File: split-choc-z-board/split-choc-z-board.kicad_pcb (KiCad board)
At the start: 2 copper layers, 122.3 x 98.6 mm, 45 parts, among them J1 USB4105-GF-A, SW1 SW_SPST, SW10 SW_SPST, SW11 SW_SPST, SW12 SW_SPST, SW13 SW_SPST, SW14 SW_SPST, SW15 SW_SPST, SW16 SW_SPST, SW17 SW_SPST, SW18 SW_SPST, SW2 SW_SPST, SW3 SW_SPST, SW4 SW_SPST, SW5 SW_SPST, SW6 SW_SPST, SW7 SW_SPST, SW8 SW_SPST, SW9 SW_SPST, U1 USBLC6-2SC6

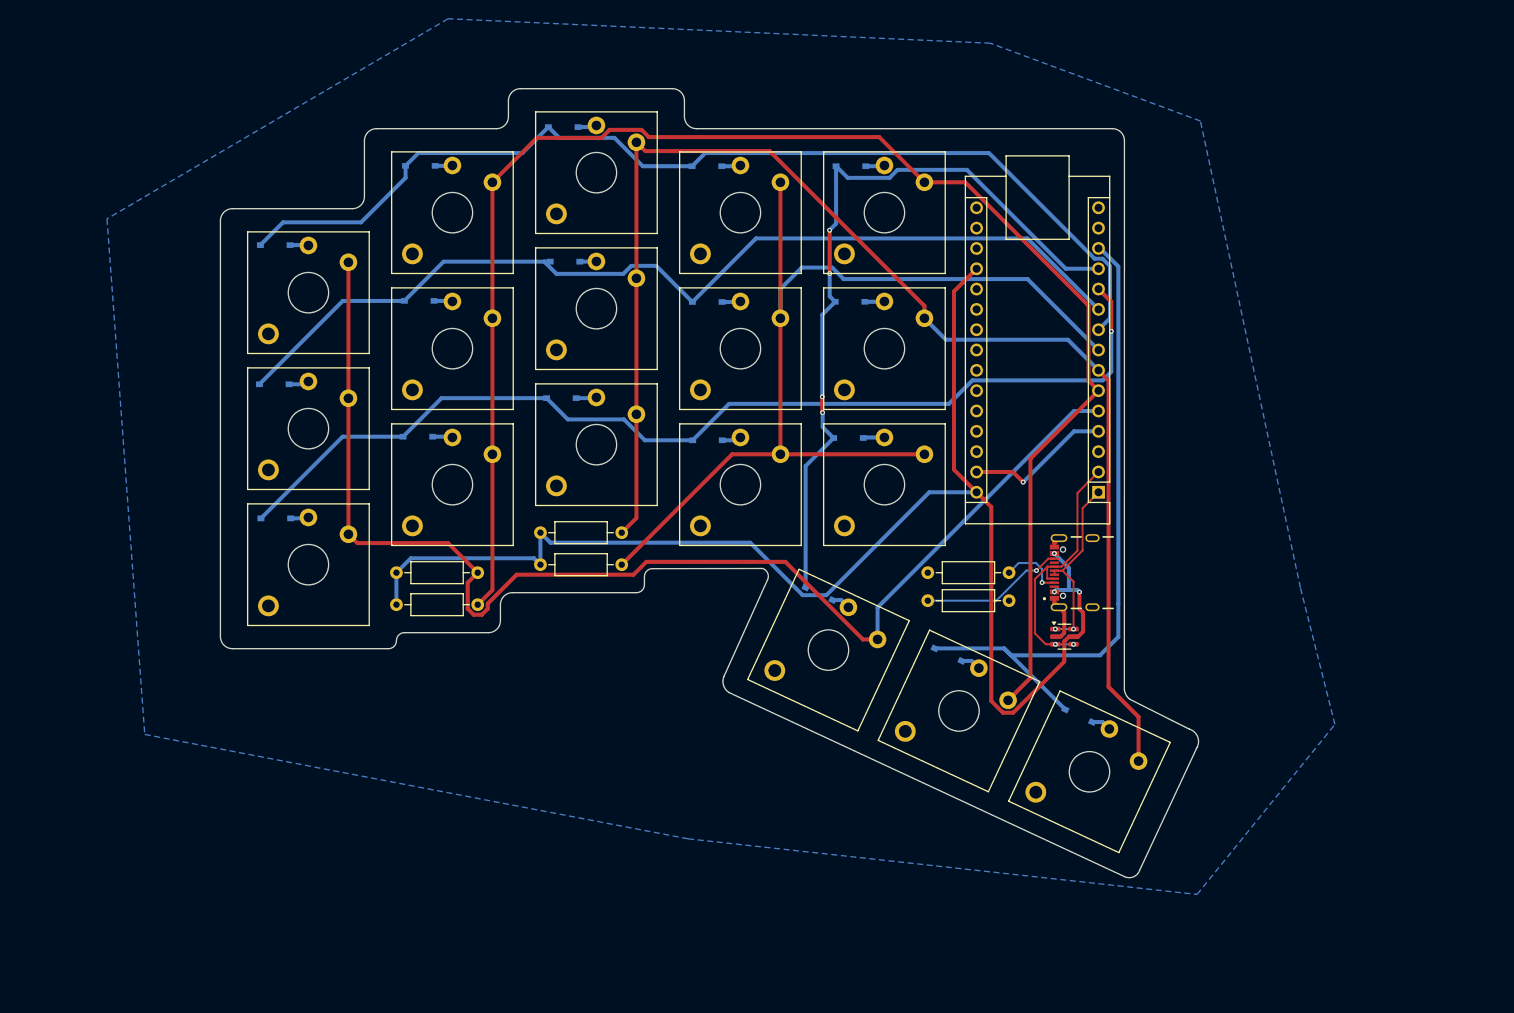
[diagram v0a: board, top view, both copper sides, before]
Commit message: Added debug pads
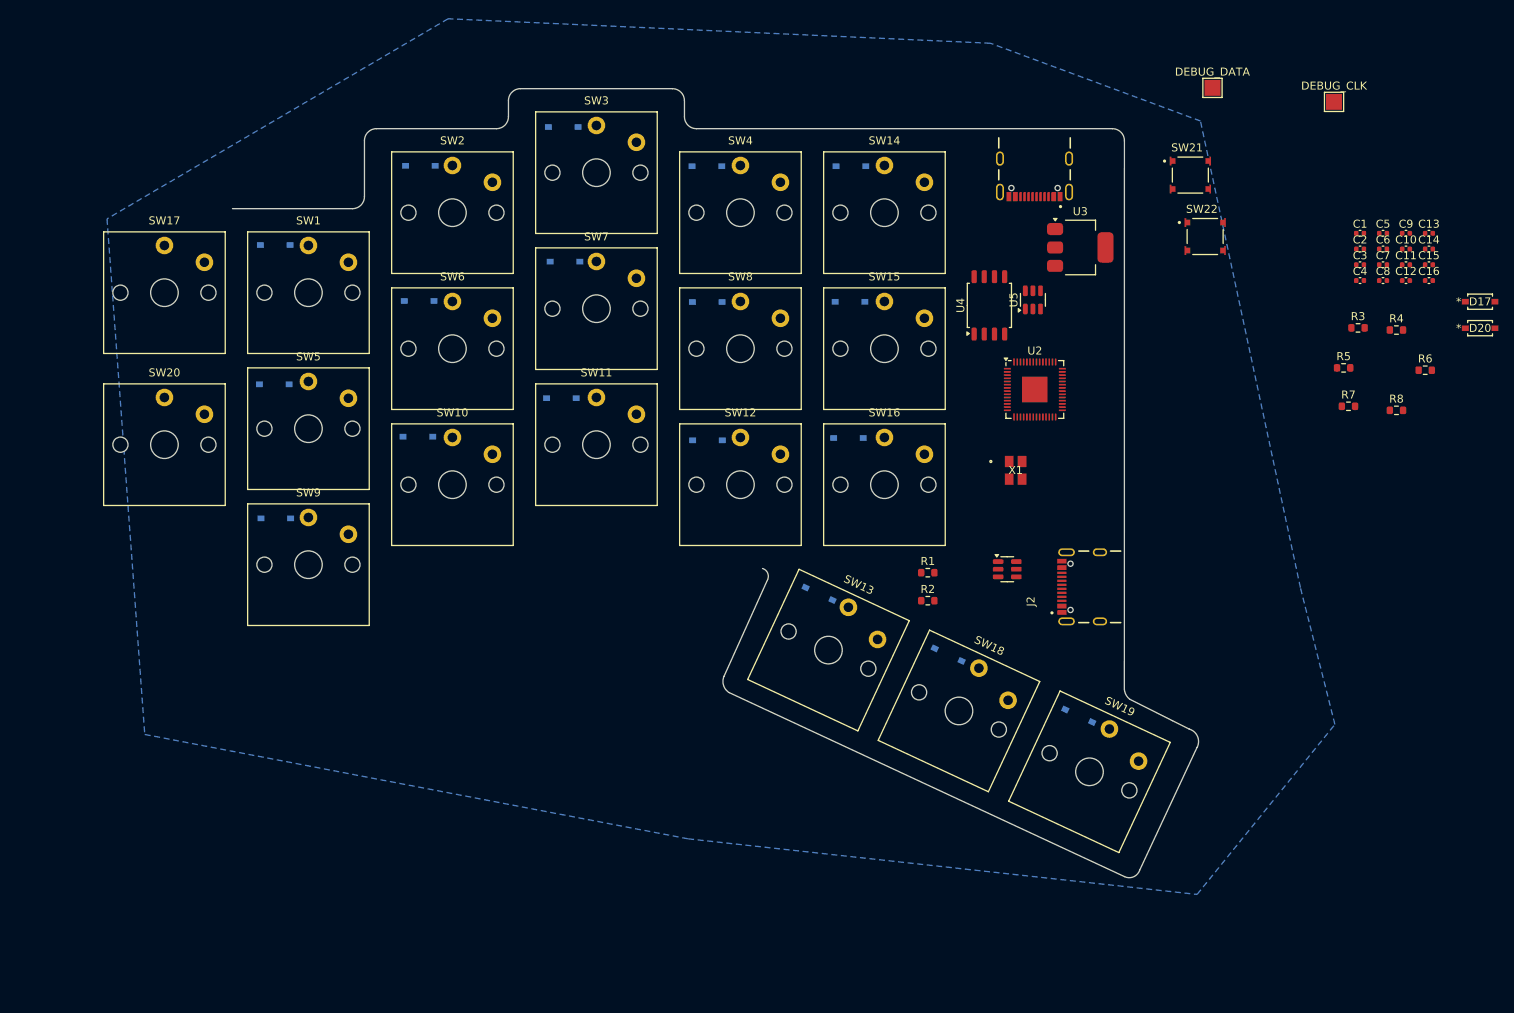
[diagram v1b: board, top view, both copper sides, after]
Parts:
- removed A1: Arduino_Nano_Every, Module:Arduino_Nano
- added C1: 1u, Capacitor_SMD:C_0402_1005Metric, F.Cu at (185.5, 58.6)
- added C10: 100n, Capacitor_SMD:C_0402_1005Metric, F.Cu at (191.2, 60.5)
- added C11: 100n, Capacitor_SMD:C_0402_1005Metric, F.Cu at (191.2, 62.5)
- added C12: 10u, Capacitor_SMD:C_0402_1005Metric, F.Cu at (191.2, 64.5)
- added C13: 10u, Capacitor_SMD:C_0402_1005Metric, F.Cu at (194.1, 58.6)
- added C14: 100n, Capacitor_SMD:C_0402_1005Metric, F.Cu at (194.1, 60.5)
- added C15: 15p, Capacitor_SMD:C_0402_1005Metric, F.Cu at (194.1, 62.5)
- added C16: 15p, Capacitor_SMD:C_0402_1005Metric, F.Cu at (194.1, 64.5)
- added C2: 100n, Capacitor_SMD:C_0402_1005Metric, F.Cu at (185.5, 60.5)
- added C3: 100n, Capacitor_SMD:C_0402_1005Metric, F.Cu at (185.5, 62.5)
- added C4: 1u, Capacitor_SMD:C_0402_1005Metric, F.Cu at (185.5, 64.5)
- added C5: 100n, Capacitor_SMD:C_0402_1005Metric, F.Cu at (188.3, 58.6)
- added C6: 100n, Capacitor_SMD:C_0402_1005Metric, F.Cu at (188.3, 60.5)
- added C7: 100n, Capacitor_SMD:C_0402_1005Metric, F.Cu at (188.3, 62.5)
- added C8: 100n, Capacitor_SMD:C_0402_1005Metric, F.Cu at (188.3, 64.5)
- added C9: 100n, Capacitor_SMD:C_0402_1005Metric, F.Cu at (191.2, 58.6)
- added D17: D, footprints:SOD123_MCC, F.Cu at (200.5, 67.1)
- added D20: D, footprints:SOD123_MCC, F.Cu at (200.5, 70.4)
- added DEBUG_CLK: MountingHole_Pad_MP, TestPoint:TestPoint_Pad_2.0x2.0mm, F.Cu at (182.2, 42.1)
- added DEBUG_DATA: MountingHole_Pad_MP, TestPoint:TestPoint_Pad_2.0x2.0mm, F.Cu at (167.0, 40.4)
- added J2: USB4105-GF-A, Library:GCT_USB4105-GF-A, F.Cu at (152.9, 102.8)
- added R7: 1k, Resistor_SMD:R_0603_1608Metric, F.Cu at (184.0, 80.2)
- added R8: 1k, Resistor_SMD:R_0603_1608Metric, F.Cu at (190.0, 80.7)
- added SW17: SW_SPST, ScottoKeebs_Choc:Choc_V1_1.00u, F.Cu at (36.0, 66.0)
- added SW20: SW_SPST, ScottoKeebs_Choc:Choc_V1_1.00u, F.Cu at (36.0, 85.0)
- added SW21: SW_SPST, Library:SW_TL3315NF250Q, F.Cu at (164.2, 51.3)
- added SW22: SW_SPST, Library:SW_TL3315NF250Q, F.Cu at (166.1, 59.0)
- added U2: RP2040, Package_DFN_QFN:QFN-56-1EP_7x7mm_P0.4mm_EP3.2x3.2mm, F.Cu at (144.8, 78.1)
- added U3: NCP1117-3.3_SOT223, Package_TO_SOT_SMD:SOT-223-3_TabPin2, F.Cu at (150.5, 60.4)
- added U4: W25Q128JVS, Package_SO:SOIC-8_5.3x5.3mm_P1.27mm, F.Cu at (139.1, 67.6)
- added U5: USBLC6-2SC6, Package_TO_SOT_SMD:SOT-23-6, F.Cu at (144.6, 66.9)
- added X1: ABM8-272-T3, Library:ABM8-272-T3_ABR, F.Cu at (142.4, 88.2)
- R1, R2: footprint Resistor_THT:R_Axial_DIN0207_L6.3mm_D2.5mm_P10.16mm_Horizontal -> Resistor_SMD:R_0603_1608Metric
- R3, R4: value R -> 27.4; footprint Resistor_THT:R_Axial_DIN0207_L6.3mm_D2.5mm_P10.16mm_Horizontal -> Resistor_SMD:R_0603_1608Metric
- R5: value R -> 10k DNP; footprint Resistor_THT:R_Axial_DIN0207_L6.3mm_D2.5mm_P10.16mm_Horizontal -> Resistor_SMD:R_0603_1608Metric
- R6: value R -> 1k; footprint Resistor_THT:R_Axial_DIN0207_L6.3mm_D2.5mm_P10.16mm_Horizontal -> Resistor_SMD:R_0603_1608Metric
- SW1, SW16, SW2, SW7, SW8, SW9: footprint ScottoKeebs_Choc:Choc_V2_1.00u -> ScottoKeebs_Choc:Choc_V1_1.00u
- SW10: renamed from SW11; footprint ScottoKeebs_Choc:Choc_V2_1.00u -> ScottoKeebs_Choc:Choc_V1_1.00u
- SW11: renamed from SW13; footprint ScottoKeebs_Choc:Choc_V2_1.00u -> ScottoKeebs_Choc:Choc_V1_1.00u
- SW12: renamed from SW15; footprint ScottoKeebs_Choc:Choc_V2_1.00u -> ScottoKeebs_Choc:Choc_V1_1.00u
- SW13: renamed from SW10; footprint ScottoKeebs_Choc:Choc_V2_1.00u -> ScottoKeebs_Choc:Choc_V1_1.00u
- SW14: renamed from SW12; footprint ScottoKeebs_Choc:Choc_V2_1.00u -> ScottoKeebs_Choc:Choc_V1_1.00u
- SW15: renamed from SW14; footprint ScottoKeebs_Choc:Choc_V2_1.00u -> ScottoKeebs_Choc:Choc_V1_1.00u
- SW18: renamed from SW17; footprint ScottoKeebs_Choc:Choc_V2_1.00u -> ScottoKeebs_Choc:Choc_V1_1.00u
- SW19: renamed from SW18; footprint ScottoKeebs_Choc:Choc_V2_1.00u -> ScottoKeebs_Choc:Choc_V1_1.00u
- SW3: renamed from SW5; footprint ScottoKeebs_Choc:Choc_V2_1.00u -> ScottoKeebs_Choc:Choc_V1_1.00u
- SW4: renamed from SW6; footprint ScottoKeebs_Choc:Choc_V2_1.00u -> ScottoKeebs_Choc:Choc_V1_1.00u
- SW5: renamed from SW3; footprint ScottoKeebs_Choc:Choc_V2_1.00u -> ScottoKeebs_Choc:Choc_V1_1.00u
- SW6: renamed from SW4; footprint ScottoKeebs_Choc:Choc_V2_1.00u -> ScottoKeebs_Choc:Choc_V1_1.00u
- moved R4 129.6 mm to (190.0, 70.7)
- moved R3 124.0 mm to (185.2, 70.4)
- moved R6 113.2 mm to (193.6, 75.7)
- moved R5 102.5 mm to (183.4, 75.4)
- moved J1 52.3 mm to (144.8, 49.2), turned to 180 degrees
- moved U1 11.1 mm to (141.3, 100.6)
- renumbered D11 to D10, D13 to D11, D15 to D12, D10 to D13, D12 to D14, D14 to D15, D17 to D18, D18 to D19, D5 to D3, D6 to D4, D3 to D5, D4 to D6
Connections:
- net /Row 1 renamed /Row_1
- net /Row 2 renamed /Row_2
- net /Row 3 renamed /Row_3
- net /Row 4 renamed /Row_4
- net /Row 5 renamed /Row_5
- J1 pad A4_B9: +5V -> VBUS
- J1 pad A6: /TX -> /USB_D+
- J1 pad A7: /TX -> /USB_D-
- J1 pad B4_A9: +5V -> VBUS
- J1 pad B6: /RX -> /USB_D+
- J1 pad B7: /RX -> /USB_D-
- R3 pad 1: +5V -> /USB_D+
- R3 pad 2: /Column 1 -> Net-(U2-USB_DP)
- R4 pad 1: +5V -> /USB_D-
- R4 pad 2: /Column 2 -> Net-(U2-USB_DM)
- R5 pad 1: +5V -> +3V3
- R5 pad 2: /Column 3 -> /QSPI_SS
- R6 pad 1: +5V -> Net-(SW21-B)
- R6 pad 2: /Column 4 -> /QSPI_SS
- SW1 pad 2: /Column 1 -> +3V3
- SW10 pad 2: /Column 2 -> +3V3
- SW11 pad 2: /Column 3 -> +3V3
- SW12 pad 2: /Column 4 -> +3V3
- SW13 pad 2: /Column 1 -> +3V3
- SW14 pad 2: /Column 2 -> +3V3
- SW15 pad 2: /Column 3 -> +3V3
- SW16 pad 2: /Column 4 -> +3V3
- SW18 pad 2: /Column 2 -> +3V3
- SW19 pad 2: /Column 3 -> +3V3
- SW2 pad 2: /Column 2 -> +3V3
- SW3 pad 2: /Column 3 -> +3V3
- SW4 pad 2: /Column 4 -> +3V3
- SW5 pad 2: /Column 1 -> +3V3
- SW6 pad 2: /Column 2 -> +3V3
- SW7 pad 2: /Column 3 -> +3V3
- SW8 pad 2: /Column 4 -> +3V3
- SW9 pad 2: /Column 1 -> +3V3
- U1 pad 1: /TX -> /USB_D+
- U1 pad 3: /RX -> /USB_D-
- U1 pad 4: /RX -> /USB_D-
- U1 pad 5: +5V -> VBUS
- U1 pad 6: /TX -> /USB_D+
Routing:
- net /Column 2: track 194.4 -> 0.00 mm
- net +5V: track 178.9 -> 0.00 mm, vias 3 -> 0
- net /Column 3: track 171.0 -> 0.00 mm
- net /Column 1: track 157.6 -> 0.00 mm
- net /Row_1: track 130.3 -> 0.00 mm
- net /Row_3: track 129.3 -> 0.00 mm, vias 1 -> 0
- net /Column 4: track 126.4 -> 0.00 mm
- net /Row_2: track 121.9 -> 0.00 mm
- net /Row_4: track 94.9 -> 0.00 mm, vias 4 -> 0
- net /Row_5: track 84.8 -> 0.00 mm
- net /RX: track 32.3 -> 0.00 mm, vias 2 -> 0
- net GND: track 25.9 -> 0.00 mm, vias 1 -> 0
- net /TX: track 23.3 -> 0.00 mm, vias 2 -> 0
- net /CC2: track 18.1 -> 0.00 mm, vias 1 -> 0
- net /CC1: track 8.17 -> 0.00 mm, vias 1 -> 0
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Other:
- board size 122.3 x 98.6 mm -> 120.8 x 98.6 mm

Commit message: Placed all components properly! 😄
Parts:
- removed DEBUG_CLK, DEBUG_DATA: MountingHole_Pad_MP, TestPoint:TestPoint_Pad_2.0x2.0mm
- removed U1: USBLC6-2SC6, Package_TO_SOT_SMD:SOT-23-6
- added C17: 100n, Capacitor_SMD:C_0402_1005Metric, F.Cu at (149.0, 84.5)
- added D_CLK1: TestPoint, TestPoint:TestPoint_Pad_D2.0mm, F.Cu at (133.0, 100.0)
- added D_DATA1: TestPoint, TestPoint:TestPoint_Pad_D2.0mm, F.Cu at (131.0, 103.0)
- added GND1: TestPoint, TestPoint:TestPoint_Pad_D2.0mm, F.Cu at (147.0, 100.0)
- added GP24: TestPoint, TestPoint:TestPoint_Pad_D2.0mm, F.Cu at (141.0, 96.0)
- added GP25: TestPoint, TestPoint:TestPoint_Pad_D2.0mm, F.Cu at (144.0, 98.0)
- D17, D20: moved to B.Cu
- moved D20 168.8 mm to (32.0, 81.0)
- moved D17 168.5 mm to (32.0, 64.0)
- moved C15 59.6 mm to (142.0, 91.5), turned to 90 degrees
- moved C13 58.3 mm to (136.0, 53.0), turned to -90 degrees
- moved R6 57.8 mm to (136.0, 71.0)
- moved C16 55.3 mm to (142.5, 84.5), turned to 90 degrees
- moved C12 54.4 mm to (138.0, 53.0), turned to -90 degrees
- moved R2 53.8 mm to (137.0, 51.0), turned to 180 degrees
- moved R1 51.8 mm to (137.0, 49.5)
- moved C7 50.3 mm to (139.5, 74.5), turned to 180 degrees
- moved C8 49.7 mm to (139.5, 73.5), turned to 180 degrees
- moved C14 49.1 mm to (145.0, 63.0)
- moved C6 48.1 mm to (145.0, 81.5), turned to -90 degrees
- moved R5 47.8 mm to (136.0, 69.5)
- moved C10 47.6 mm to (144.5, 70.0), turned to 90 degrees
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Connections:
- C10 pad 1: +3.3V -> +3V3
- C11 pad 1: +3.3V -> +3V3
- C5 pad 1: +3.3V -> +3V3
- C6 pad 1: +3.3V -> +3V3
- C7 pad 1: +3.3V -> +3V3
- C8 pad 1: +3.3V -> +3V3
- C9 pad 1: +3.3V -> +3V3
- SW1 pad 2: +3V3 -> /Col_1
- SW10 pad 2: +3V3 -> /Col_2
- SW11 pad 2: +3V3 -> /Col_3
- SW12 pad 2: +3V3 -> /Col_4
- SW13 pad 2: +3V3 -> /Col_1
- SW14 pad 2: +3V3 -> /Col_2
- SW15 pad 2: +3V3 -> /Col_3
- SW16 pad 2: +3V3 -> /Col_4
- SW17 pad 2: +3V3 -> /Col_1
- SW18 pad 2: +3V3 -> /Col_2
- SW19 pad 2: +3V3 -> /Col_3
- SW2 pad 2: +3V3 -> /Col_2
- SW20 pad 2: +3V3 -> /Col_4
- SW3 pad 2: +3V3 -> /Col_3
- SW4 pad 2: +3V3 -> /Col_4
- SW5 pad 2: +3V3 -> /Col_1
- SW6 pad 2: +3V3 -> /Col_2
- SW7 pad 2: +3V3 -> /Col_3
- SW8 pad 2: +3V3 -> /Col_4
- SW9 pad 2: +3V3 -> /Col_1
- U2 pad 3: +3V3 -> /Col_1
- U2 pad 36: unconnected-(U2-GPIO24-Pad36) -> /GP24
- U2 pad 37: unconnected-(U2-GPIO25-Pad37) -> /GP25
- U2 pad 4: +3V3 -> /Col_2
- U2 pad 5: +3V3 -> /Col_3
- U2 pad 6: +3V3 -> /Col_4
- U5 pad 1: /USB_D+ -> /B-B_D+
- U5 pad 3: /USB_D- -> /B-B_D-
- U5 pad 4: /USB_D- -> /B-B_D-
- U5 pad 6: /USB_D+ -> /B-B_D+
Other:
- board outline removed

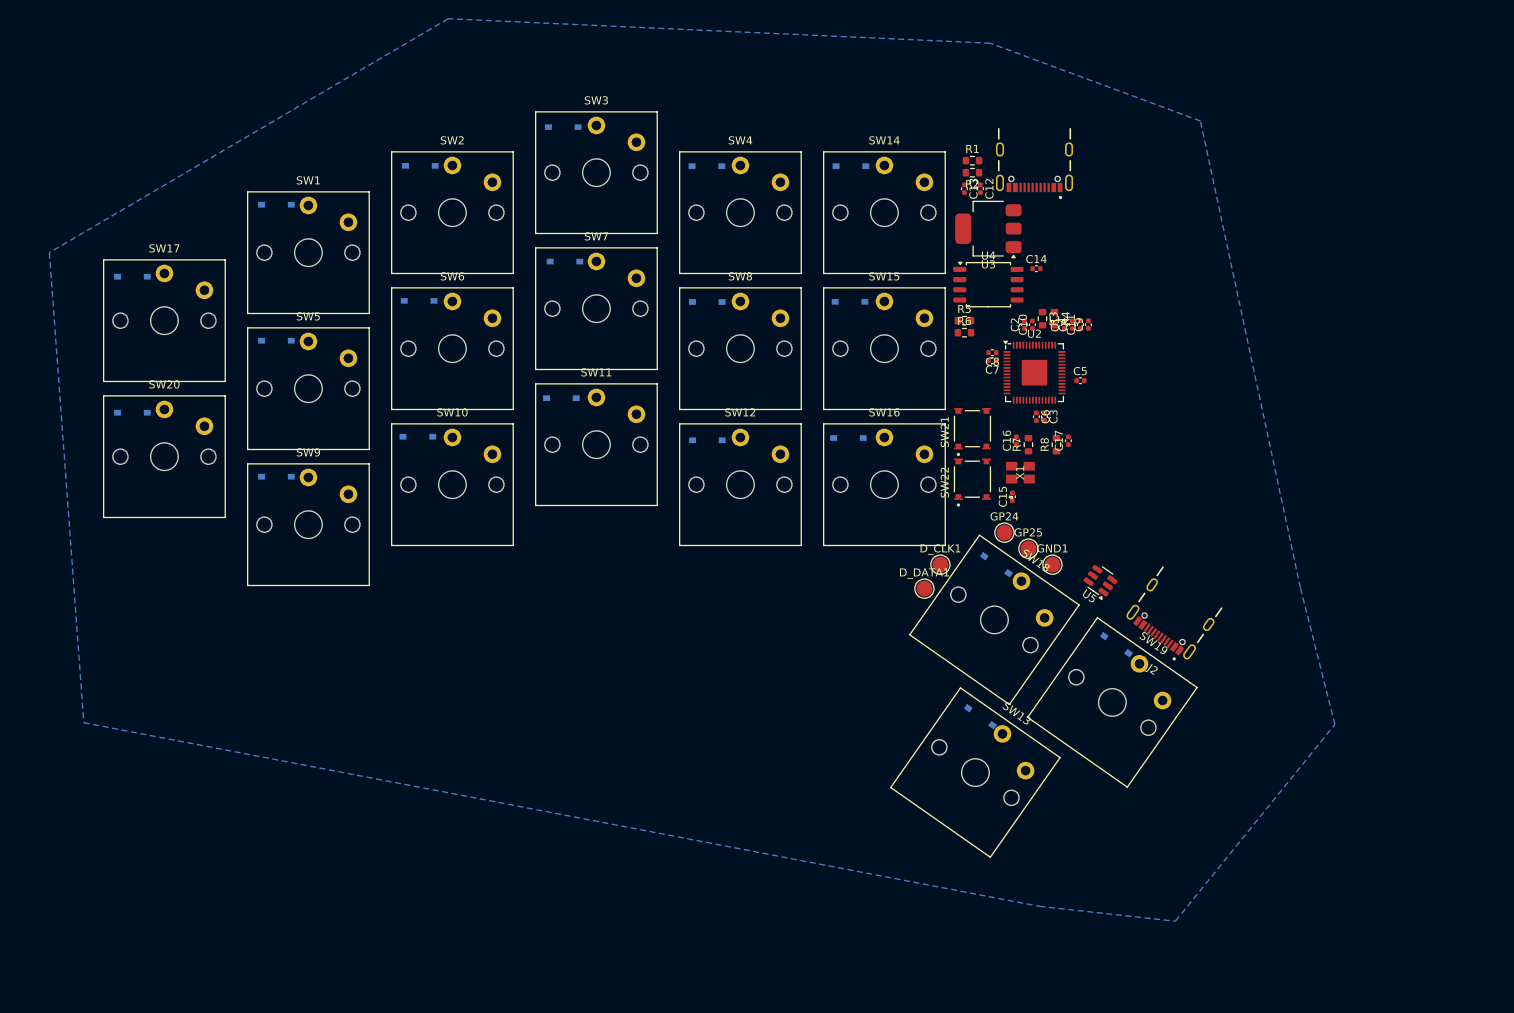
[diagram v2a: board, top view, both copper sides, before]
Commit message: Finished board outline 🖥️
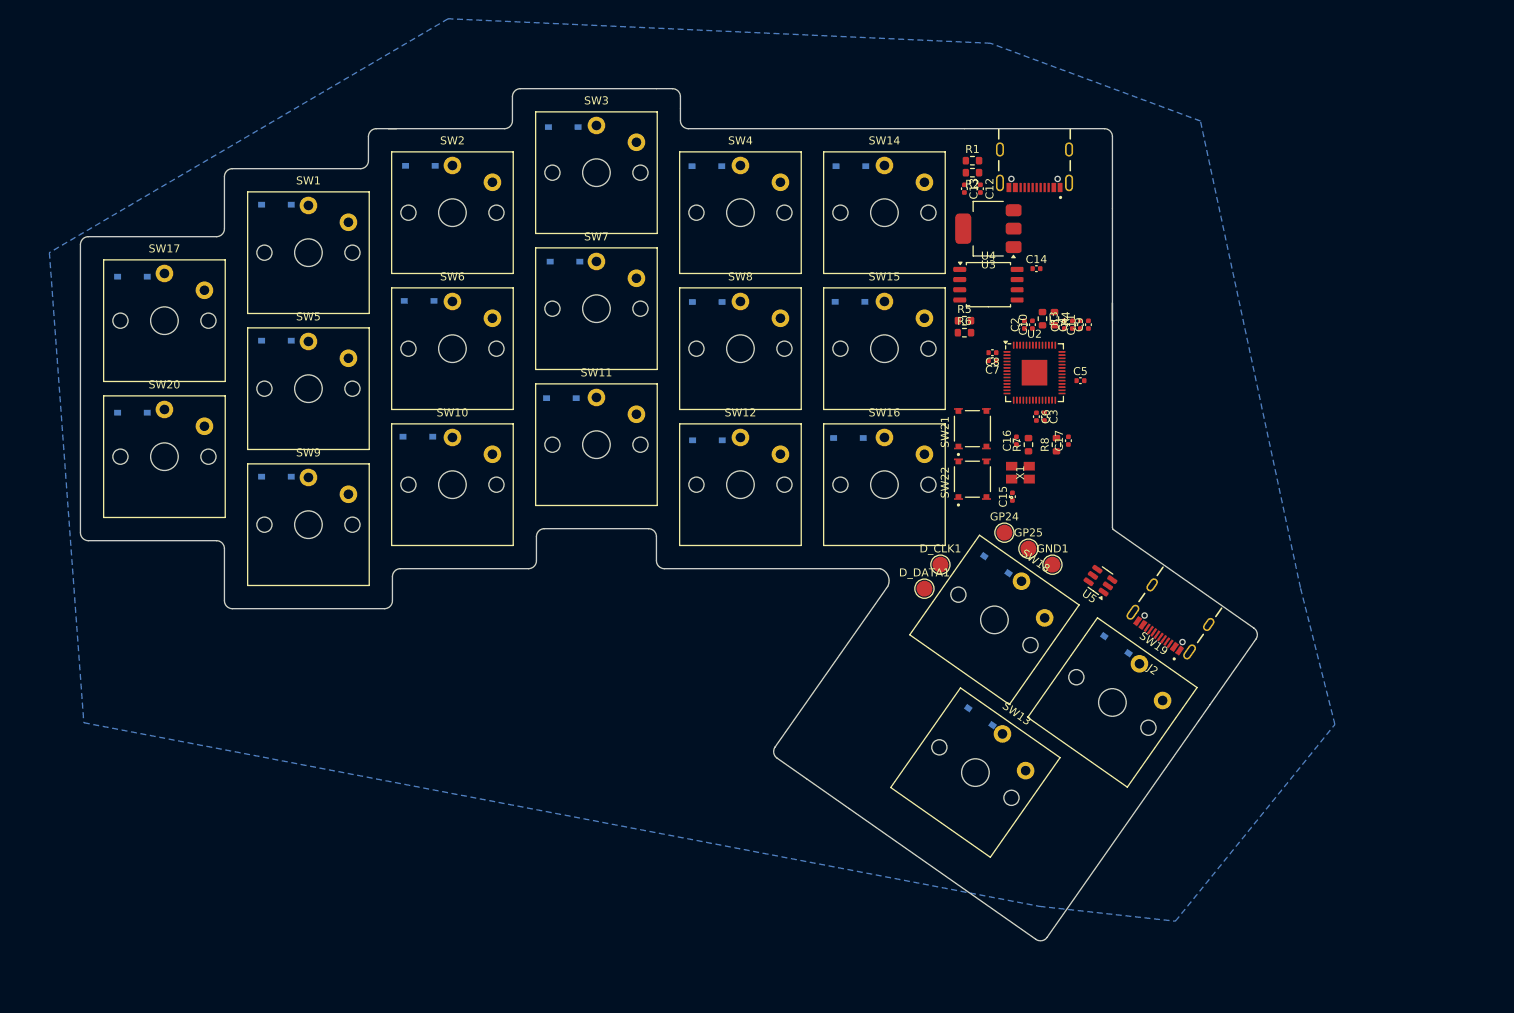
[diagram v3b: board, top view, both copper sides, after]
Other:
- board outline added: 147.1 x 106.5 mm
